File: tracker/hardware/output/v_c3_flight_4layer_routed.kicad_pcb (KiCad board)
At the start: 4 copper layers, 55 x 45 mm, 20 parts, among them J1 Prog_Header, J2 Debug_Header, U1 ESP32-C3-WROOM-02, U2 LR2021F33, U3 MAX-M10S, U4 TPS7A02, U5 BMP280

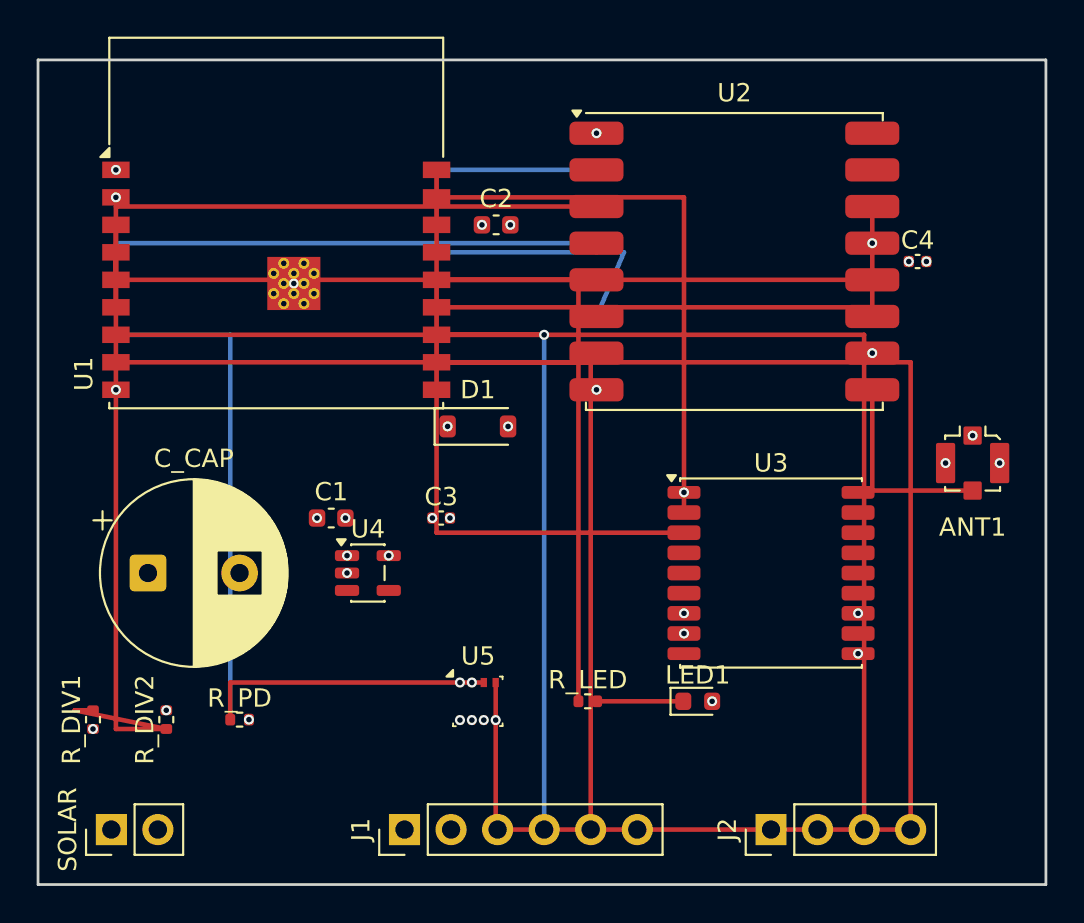
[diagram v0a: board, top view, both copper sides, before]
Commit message: feat(pcb): 4-layer conversion with GND/3V3 power planes + collision-aware routing
- Enable In1.Cu (GND plane) and In2.Cu (+3V3 plane) as power planes
- Rip all existing tracks, re-route 17 signal nets across F.Cu + B.Cu
- Manhattan routing with Liang-Barsky bbox collision detection
- Thermal vias at SMD power pads (skip THT)
- Dual-layer distribution: try both layers, pick fewer collisions
- DRC: 0 tracks_crossing, 0 shorts, 0 solder_mask_bridge (was 12/1/0)
- Remaining: 20 unconnected, 3 clearance, 5 dangling vias
- Placement audit: 14 footprint overlaps found (root cause of remaining issues)

Co-Authored-By: balloon-circuit-design worker
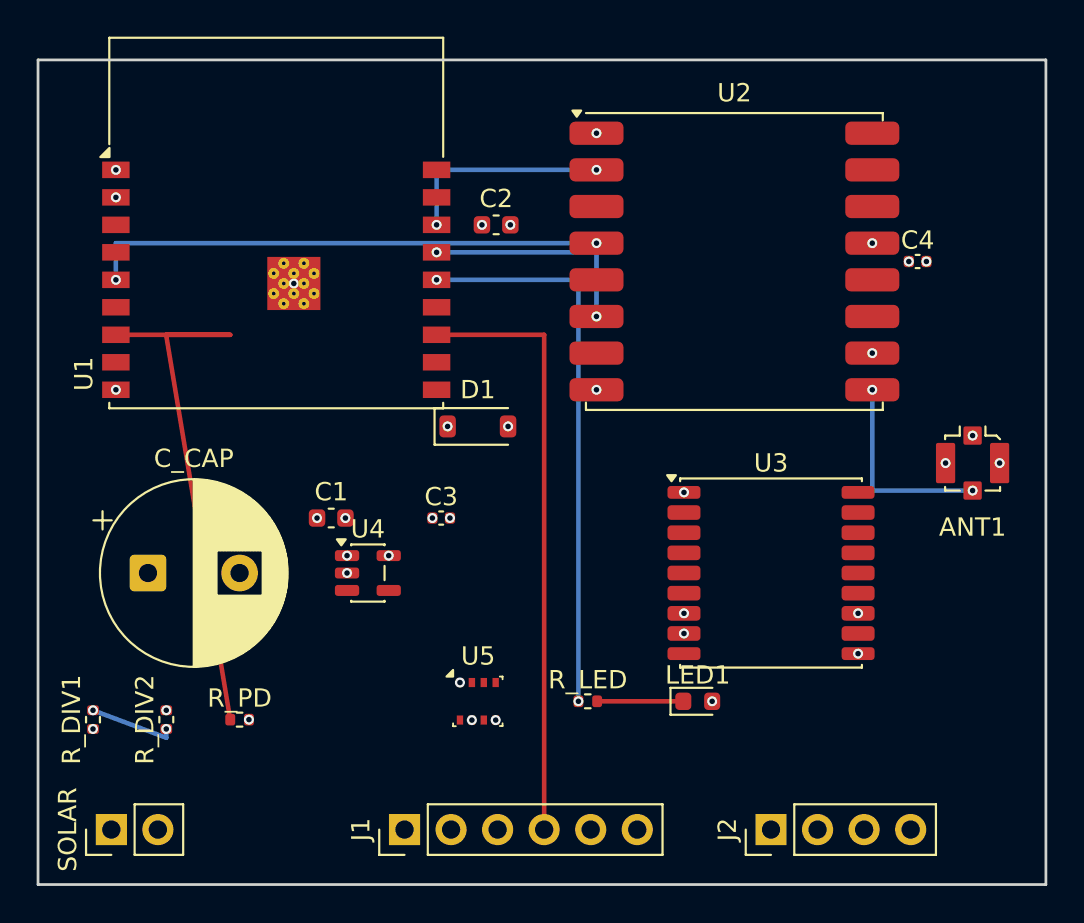
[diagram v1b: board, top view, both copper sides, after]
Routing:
- net I2C_SCL: track 99.5 -> 0.00 mm
- net I2C_SDA: track 83.7 -> 31.0 mm
- net LR_BUSY: track 44.3 -> 0.00 mm
- net UART0_RX: track 33.9 -> 0.00 mm
- net GPS_TX: track 33.3 -> 0.00 mm
- net SPI_MOSI: track 31.7 -> 0.00 mm
- net GPS_RX: track 30.7 -> 0.00 mm
- net VDIV_MID: track 34.9 -> 4.75 mm, vias 0 -> 2
- net LR_DIO0: track 29.3 -> 0.00 mm
- net GND: track 27.2 -> 0.00 mm, vias 37 -> 21
- net SPI_NSS: track 14.7 -> 0.00 mm
- net LR_RST: track 14.0 -> 12.2 mm, vias 0 -> 2
- net VCAP: vias 4 -> 3
- net UART0_TX: vias 1 -> 0
- net SPI_SCK: vias 0 -> 2
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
